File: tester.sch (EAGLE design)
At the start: 73 parts, among them IC1 ATmega8/88/168, K1 NA 05W K, M1 SP6000C-180, P1 250, P2 10k lin, Q1 BC847CSMD, Q2 BC847CSMD, Q3 BC328-40, Q4 8,000 MHz, Q5 BC847CSMD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

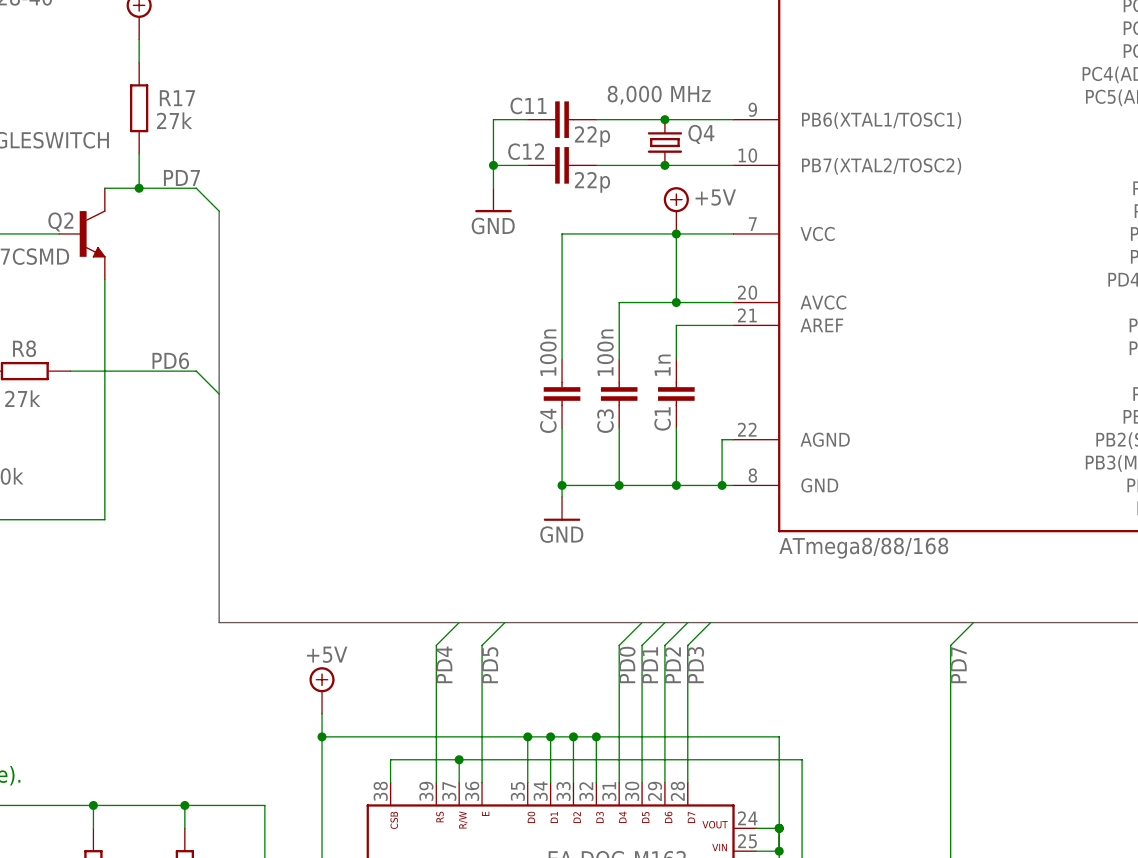
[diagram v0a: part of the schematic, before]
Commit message: switched lcd wiring to streifenraster
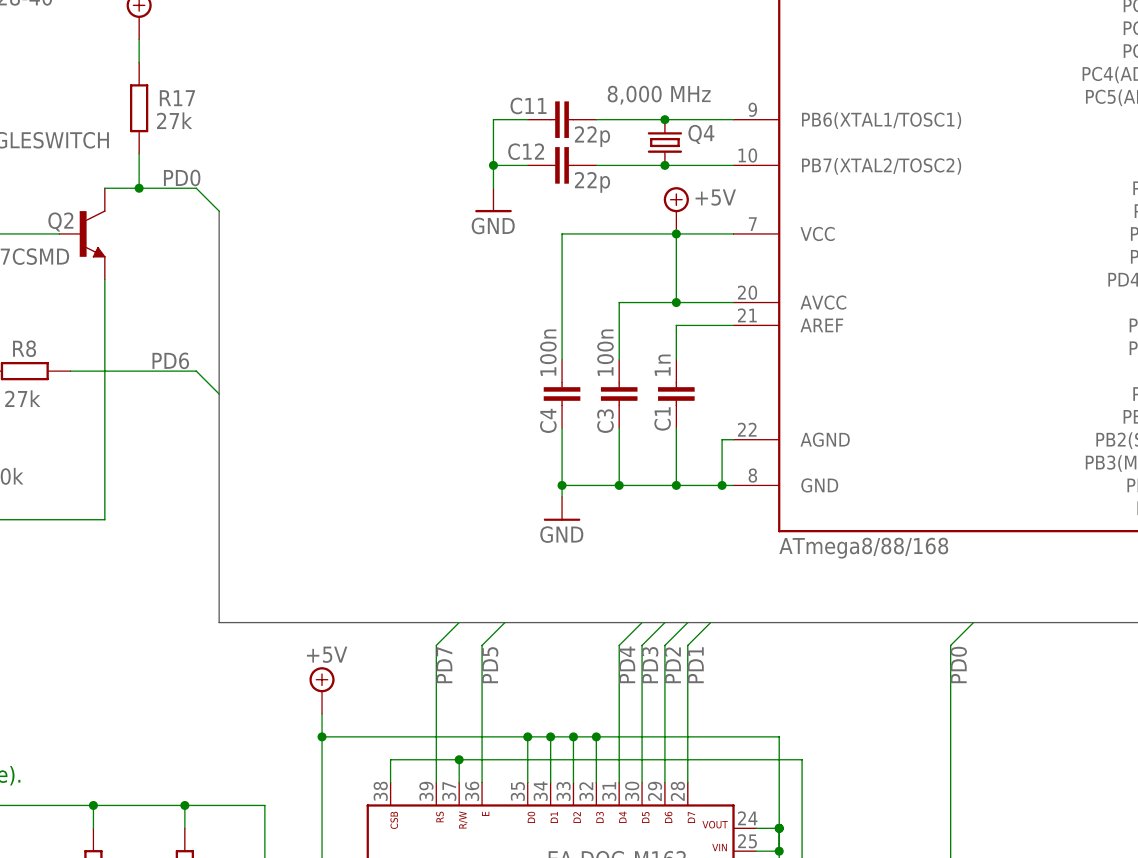
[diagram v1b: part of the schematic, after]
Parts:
- R1, R2, R28, R29, R3, R4, R5, R6: device resistor:R-EU_R0603 -> resistor:R-EU_R0805
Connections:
- net PD0: now also Q2.C, Q9.G, R17.1; no longer DIS1.31
- net PD1: now also DIS1.28; no longer DIS1.30
- net PD3: now also DIS1.30; no longer DIS1.28
- net PD4: now also DIS1.31; no longer DIS1.39
- net PD7: now also DIS1.39; no longer Q2.C, Q9.G, R17.1
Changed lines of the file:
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@@
 <setting verticaltext="up"/>
 </settings>
-<grid distance="0.1" unitdist="inch" unit="mm" style="lines" multiple="1" display="yes" altdistance="0.01" altunitdist="inch" altunit="mm"/>
+<grid distance="1.27" unitdist="mm" unit="mm" style="lines" multiple="1" display="yes" altdistance="635" altunitdist="mic" altunit="mic"/>
 <layers>
 <layer number="1" name="Top" color="4" fill="1" visible="yes" active="no"/>
@@
 <part name="R9" library="resistor" deviceset="R-EU_" device="R0603" value="100k"/>
 <part name="C2" library="rcl" deviceset="C-EU" device="C0603" value="10n"/>
-<part name="R1" library="resistor" deviceset="R-EU_" device="R0603" value="680">
+<part name="R1" library="resistor" deviceset="R-EU_" device="R0805" value="680">
 <attribute name="TOLERANCE" value="0.1%"/>
 </part>
-<part name="R2" library="resistor" deviceset="R-EU_" device="R0603" value="470k">
+<part name="R2" library="resistor" deviceset="R-EU_" device="R0805" value="470k">
 <attribute name="TOLERANCE" value="0.1%"/>
 </part>
-<part name="R3" library="resistor" deviceset="R-EU_" device="R0603" value="680">
+<part name="R3" library="resistor" deviceset="R-EU_" device="R0805" value="680">
 <attribute name="TOLERANCE" value="0.1%"/>
 </part>
-<part name="R4" library="resistor" deviceset="R-EU_" device="R0603" value="470k">
+<part name="R4" library="resistor" deviceset="R-EU_" device="R0805" value="470k">
 <attribute name="TOLERANCE" value="0.1%"/>
 </part>
-<part name="R5" library="resistor" deviceset="R-EU_" device="R0603" value="680">
+<part name="R5" library="resistor" deviceset="R-EU_" device="R0805" value="680">
 <attribute name="TOLERANCE" value="0.1%"/>
 </part>
-<part name="R6" library="resistor" deviceset="R-EU_" device="R0603" value="470k">
+<part name="R6" library="resistor" deviceset="R-EU_" device="R0805" value="470k">
 <attribute name="TOLERANCE" value="0.1%"/>
 </part>
@@
 <part name="DC1" library="dc-dc-converter" deviceset="NMA" device="" value="5V/+-15V"/>
 <part name="R26" library="resistor" deviceset="R-EU_" device="R0603" value="10k"/>
-<part name="R28" library="resistor" deviceset="R-EU_" device="R0603" value="180k">
+<part name="R28" library="resistor" deviceset="R-EU_" device="R0805" value="180k">
 <attribute name="TOLERANCE" value="0.1%"/>
 </part>
-<part name="R29" library="resistor" deviceset="R-EU_" device="R0603" value="20k">
+<part name="R29" library="resistor" deviceset="R-EU_" device="R0805" value="20k">
 <attribute name="TOLERANCE" value="0.1%"/>
 </part>
@@
 <segment>
 <wire x1="238.76" y1="157.48" x2="236.22" y2="160.02" width="0.1524" layer="91"/>
+<pinref part="IC1" gate="1" pin="PD7(AIN1)"/>
 <wire x1="236.22" y1="160.02" x2="231.14" y2="160.02" width="0.1524" layer="91"/>
-<pinref part="IC1" gate="1" pin="PD7(AIN1)"/>
+</segment>
+<segment>
+<wire x1="139.7" y1="129.54" x2="137.16" y2="127" width="0.1524" layer="91"/>
+<label x="137.16" y="127" size="1.778" layer="95" rot="R270"/>
+<pinref part="DIS1" gate="G$1" pin="39"/>
+<wire x1="137.16" y1="111.76" x2="137.16" y2="127" width="0.1524" layer="91"/>
+</segment>
+</net>
+<net name="PD6" class="0">
+<segment>
+<wire x1="238.76" y1="160.02" x2="236.22" y2="162.56" width="0.1524" layer="91"/>
+<wire x1="236.22" y1="162.56" x2="231.14" y2="162.56" width="0.1524" layer="91"/>
+<pinref part="IC1" gate="1" pin="PD6(AIN0)"/>
+</segment>
+<segment>
+<wire x1="113.03" y1="154.94" x2="110.49" y2="157.48" width="0.1524" layer="91"/>
+<pinref part="R8" gate="G$1" pin="1"/>
+<label x="105.41" y="157.734" size="1.778" layer="95"/>
+<wire x1="110.49" y1="157.48" x2="96.52" y2="157.48" width="0.1524" layer="91"/>
+</segment>
+</net>
+<net name="PD1" class="0">
+<segment>
+<wire x1="238.76" y1="172.72" x2="236.22" y2="175.26" width="0.1524" layer="91"/>
+<pinref part="IC1" gate="1" pin="PD1(TXD)"/>
+<wire x1="236.22" y1="175.26" x2="231.14" y2="175.26" width="0.1524" layer="91"/>
+</segment>
+<segment>
+<wire x1="167.64" y1="129.54" x2="165.1" y2="127" width="0.1524" layer="91"/>
+<wire x1="165.1" y1="127" x2="165.1" y2="111.76" width="0.1524" layer="91"/>
+<label x="165.1" y="127" size="1.778" layer="95" rot="R270"/>
+<pinref part="DIS1" gate="G$1" pin="28"/>
+</segment>
+</net>
+<net name="PD0" class="0">
+<segment>
+<wire x1="238.76" y1="175.26" x2="236.22" y2="177.8" width="0.1524" layer="91"/>
+<pinref part="IC1" gate="1" pin="PD0(RXD)"/>
+<wire x1="236.22" y1="177.8" x2="231.14" y2="177.8" width="0.1524" layer="91"/>
 </segment>
 <segment>
@@
 </segment>
 <segment>
-<wire x1="196.85" y1="129.54" x2="194.31" y2="127" width="0.1524" layer="91"/>
 <pinref part="Q9" gate="G$1" pin="G"/>
 <wire x1="194.31" y1="127" x2="194.31" y2="82.55" width="0.1524" layer="91"/>
 <label x="194.31" y="127" size="1.778" layer="95" rot="R270"/>
-</segment>
-</net>
-<net name="PD6" class="0">
-<segment>
-<wire x1="238.76" y1="160.02" x2="236.22" y2="162.56" width="0.1524" layer="91"/>
-<wire x1="236.22" y1="162.56" x2="231.14" y2="162.56" width="0.1524" layer="91"/>
-<pinref part="IC1" gate="1" pin="PD6(AIN0)"/>
-</segment>
-<segment>
-<wire x1="113.03" y1="154.94" x2="110.49" y2="157.48" width="0.1524" layer="91"/>
-<pinref part="R8" gate="G$1" pin="1"/>
-<label x="105.41" y="157.734" size="1.778" layer="95"/>
-<wire x1="110.49" y1="157.48" x2="96.52" y2="157.48" width="0.1524" layer="91"/>
-</segment>
-</net>
-<net name="PD1" class="0">
-<segment>
-<wire x1="238.76" y1="172.72" x2="236.22" y2="175.26" width="0.1524" layer="91"/>
-<wire x1="236.22" y1="175.26" x2="231.14" y2="175.26" width="0.1524" layer="91"/>
-<pinref part="IC1" gate="1" pin="PD1(TXD)"/>
+<wire x1="196.85" y1="129.54" x2="194.31" y2="127" width="0.1524" layer="91"/>
+</segment>
+</net>
+<net name="PD2" class="0">
+<segment>
+<wire x1="238.76" y1="170.18" x2="236.22" y2="172.72" width="0.1524" layer="91"/>
+<wire x1="236.22" y1="172.72" x2="231.14" y2="172.72" width="0.1524" layer="91"/>
+<pinref part="IC1" gate="1" pin="PD2(INT0)"/>
+</segment>
+<segment>
+<wire x1="165.1" y1="129.54" x2="162.56" y2="127" width="0.1524" layer="91"/>
+<label x="162.56" y="127" size="1.778" layer="95" rot="R270"/>
+<pinref part="DIS1" gate="G$1" pin="29"/>
+<wire x1="162.56" y1="111.76" x2="162.56" y2="127" width="0.1524" layer="91"/>
+</segment>
+</net>
+<net name="PD3" class="0">
+<segment>
+<wire x1="238.76" y1="167.64" x2="236.22" y2="170.18" width="0.1524" layer="91"/>
+<pinref part="IC1" gate="1" pin="PD3(INT1)"/>
+<wire x1="236.22" y1="170.18" x2="231.14" y2="170.18" width="0.1524" layer="91"/>
 </segment>
 <segment>
@@
 </segment>
 </net>
-<net name="PD0" class="0">
-<segment>
-<wire x1="238.76" y1="175.26" x2="236.22" y2="177.8" width="0.1524" layer="91"/>
-<wire x1="236.22" y1="177.8" x2="231.14" y2="177.8" width="0.1524" layer="91"/>
-<pinref part="IC1" gate="1" pin="PD0(RXD)"/>
+<net name="PD4" class="0">
+<segment>
+<wire x1="238.76" y1="165.1" x2="236.22" y2="167.64" width="0.1524" layer="91"/>
+<pinref part="IC1" gate="1" pin="PD4(T0/XCK)"/>
+<wire x1="236.22" y1="167.64" x2="231.14" y2="167.64" width="0.1524" layer="91"/>
 </segment>
 <segment>
@@
 </segment>
 </net>
-<net name="PD2" class="0">
-<segment>
-<wire x1="238.76" y1="170.18" x2="236.22" y2="172.72" width="0.1524" layer="91"/>
-<wire x1="236.22" y1="172.72" x2="231.14" y2="172.72" width="0.1524" layer="91"/>
-<pinref part="IC1" gate="1" pin="PD2(INT0)"/>
-</segment>
-<segment>
-<wire x1="165.1" y1="129.54" x2="162.56" y2="127" width="0.1524" layer="91"/>
-<label x="162.56" y="127" size="1.778" layer="95" rot="R270"/>
-<pinref part="DIS1" gate="G$1" pin="29"/>
-<wire x1="162.56" y1="111.76" x2="162.56" y2="127" width="0.1524" layer="91"/>
-</segment>
-</net>
-<net name="PD3" class="0">
-<segment>
-<wire x1="238.76" y1="167.64" x2="236.22" y2="170.18" width="0.1524" layer="91"/>
-<wire x1="236.22" y1="170.18" x2="231.14" y2="170.18" width="0.1524" layer="91"/>
-<pinref part="IC1" gate="1" pin="PD3(INT1)"/>
-</segment>
-<segment>
-<wire x1="167.64" y1="129.54" x2="165.1" y2="127" width="0.1524" layer="91"/>
-<wire x1="165.1" y1="127" x2="165.1" y2="111.76" width="0.1524" layer="91"/>
-<label x="165.1" y="127" size="1.778" layer="95" rot="R270"/>
-<pinref part="DIS1" gate="G$1" pin="28"/>
-</segment>
-</net>
-<net name="PD4" class="0">
-<segment>
-<wire x1="238.76" y1="165.1" x2="236.22" y2="167.64" width="0.1524" layer="91"/>
-<wire x1="236.22" y1="167.64" x2="231.14" y2="167.64" width="0.1524" layer="91"/>
-<pinref part="IC1" gate="1" pin="PD4(T0/XCK)"/>
-</segment>
-<segment>
-<wire x1="139.7" y1="129.54" x2="137.16" y2="127" width="0.1524" layer="91"/>
-<label x="137.16" y="127" size="1.778" layer="95" rot="R270"/>
-<pinref part="DIS1" gate="G$1" pin="39"/>
-<wire x1="137.16" y1="111.76" x2="137.16" y2="127" width="0.1524" layer="91"/>
-</segment>
-</net>

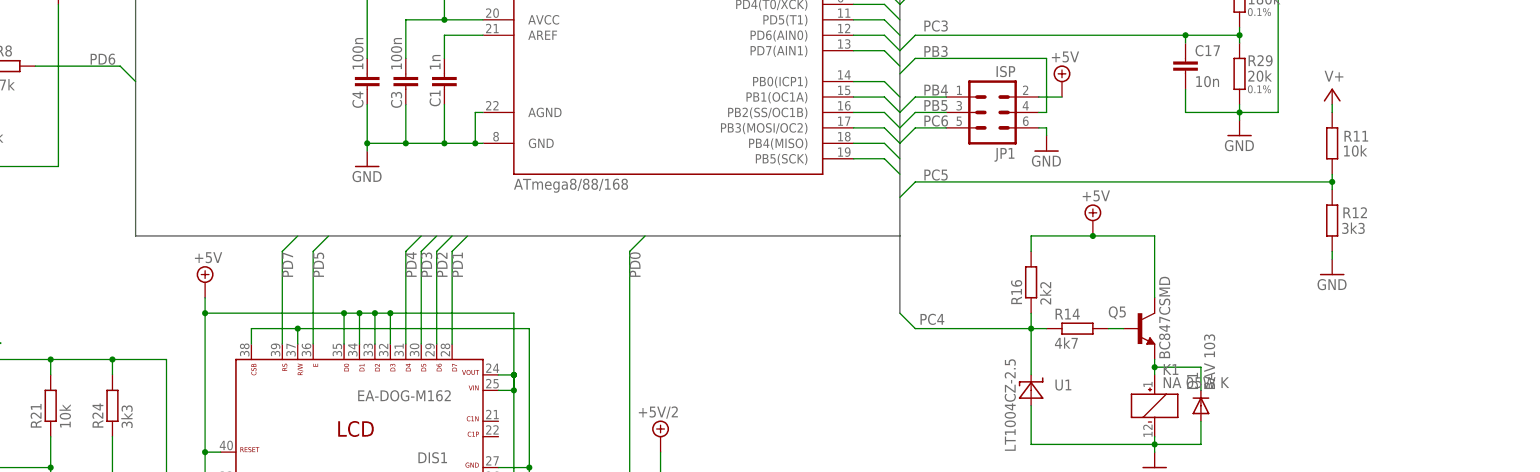
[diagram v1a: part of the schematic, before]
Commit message: power lcd bg led directly from v+
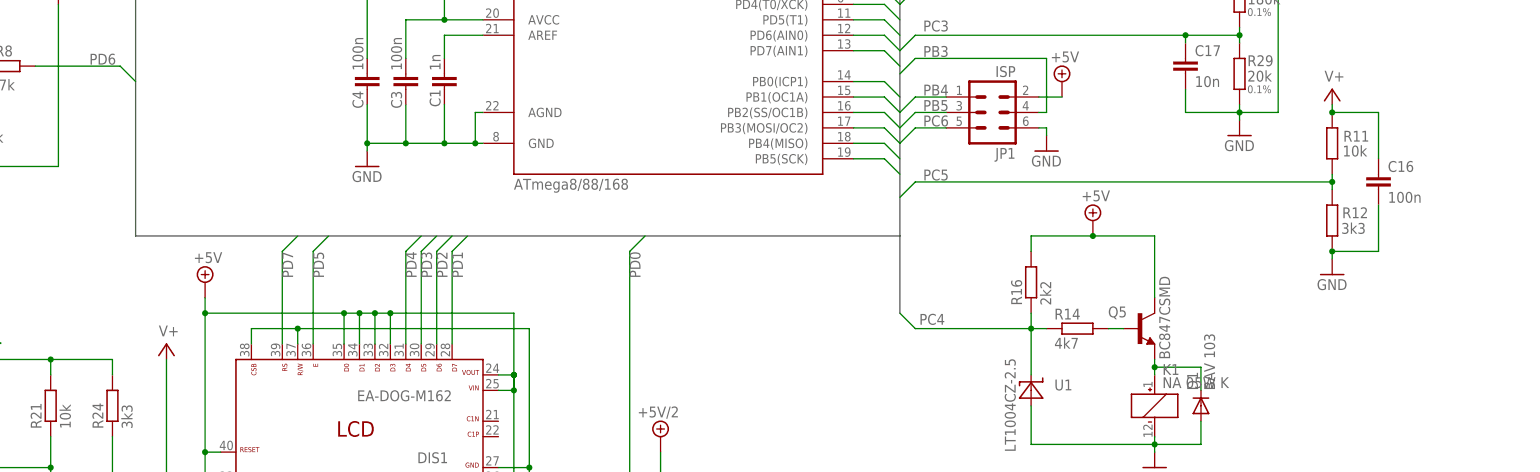
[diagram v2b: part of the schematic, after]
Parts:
- added C16: 100n, rcl:C-EUC0603
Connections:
- net +5V/2: no longer DIS1.1, DIS1.20
- net GND: now also C16.2
- net V+: now also C16.1, DIS1.1, DIS1.20
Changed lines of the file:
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@@
 <part name="PLATINENSAMMLER" library="Platinensammler" deviceset="LP_NUMBER" device="08_SILK_TOP"/>
 <part name="JP7" library="con-lsta" deviceset="FE02-1" device="" value="TEST2"/>
+<part name="SUPPLY5" library="supply2" deviceset="V+" device=""/>
+<part name="C16" library="rcl" deviceset="C-EU" device="C0603" value="100n"/>
 </parts>
 <sheets>
@@
 <instance part="PLATINENSAMMLER" gate="G$1" x="351.79" y="248.92"/>
 <instance part="JP7" gate="G$1" x="284.48" y="228.6" rot="R270"/>
+<instance part="SUPPLY5" gate="1" x="118.11" y="111.76"/>
+<instance part="C16" gate="G$1" x="317.5" y="139.7"/>
 </instances>
 <busses>
@@
 <wire x1="309.88" y1="125.73" x2="309.88" y2="127" width="0.1524" layer="91"/>
 <pinref part="GND11" gate="1" pin="GND"/>
+<pinref part="C16" gate="G$1" pin="2"/>
+<wire x1="309.88" y1="127" x2="317.5" y2="127" width="0.1524" layer="91"/>
+<wire x1="317.5" y1="127" x2="317.5" y2="134.62" width="0.1524" layer="91"/>
+<junction x="309.88" y="127"/>
 </segment>
 <segment>
@@
 <wire x1="27.94" y1="83.82" x2="27.94" y2="109.22" width="0.1524" layer="91"/>
 <junction x="27.94" y="109.22"/>
-<junction x="109.22" y="109.22"/>
-<pinref part="DIS1" gate="G$1" pin="20"/>
-<wire x1="157.48" y1="81.28" x2="118.11" y2="81.28" width="0.1524" layer="91"/>
-<wire x1="118.11" y1="81.28" x2="118.11" y2="109.22" width="0.1524" layer="91"/>
-<wire x1="118.11" y1="109.22" x2="109.22" y2="109.22" width="0.1524" layer="91"/>
-<wire x1="157.48" y1="83.82" x2="157.48" y2="81.28" width="0.1524" layer="91"/>
-<pinref part="DIS1" gate="G$1" pin="1"/>
-<wire x1="165.1" y1="83.82" x2="165.1" y2="81.28" width="0.1524" layer="91"/>
-<wire x1="165.1" y1="81.28" x2="157.48" y2="81.28" width="0.1524" layer="91"/>
-<junction x="157.48" y="81.28"/>
 <pinref part="P+4" gate="G$1" pin="+5V/2"/>
 <wire x1="17.78" y1="111.76" x2="17.78" y2="109.22" width="0.1524" layer="91"/>
@@
 <wire x1="309.88" y1="149.86" x2="309.88" y2="151.13" width="0.1524" layer="91"/>
 <pinref part="SUPPLY9" gate="1" pin="V+"/>
-</segment>
-</net>
+<pinref part="C16" gate="G$1" pin="1"/>
+<wire x1="317.5" y1="142.24" x2="317.5" y2="149.86" width="0.1524" layer="91"/>
+<wire x1="317.5" y1="149.86" x2="309.88" y2="149.86" width="0.1524" layer="91"/>
+<junction x="309.88" y="149.86"/>
+</segment>
+<segment>
+<pinref part="DIS1" gate="G$1" pin="20"/>
+<wire x1="157.48" y1="83.82" x2="157.48" y2="81.28" width="0.1524" layer="91"/>
+<pinref part="DIS1" gate="G$1" pin="1"/>
+<wire x1="165.1" y1="83.82" x2="165.1" y2="81.28" width="0.1524" layer="91"/>
+<wire x1="165.1" y1="81.28" x2="157.48" y2="81.28" width="0.1524" layer="91"/>
+<junction x="157.48" y="81.28"/>
+<wire x1="157.48" y1="81.28" x2="118.11" y2="81.28" width="0.1524" layer="91"/>
+<wire x1="118.11" y1="81.28" x2="118.11" y2="109.22" width="0.1524" layer="91"/>
+<pinref part="SUPPLY5" gate="1" pin="V+"/>
+</segment>
+</net>
